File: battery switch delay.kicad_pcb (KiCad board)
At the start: 2 copper layers, 35.5 x 56 mm, 15 parts, among them J1 5mm pitch 4 position screw te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, K2 G6E-134P-US, Q1 Q_NPN, U2 MIC2920A-12WS-TR_SOT223

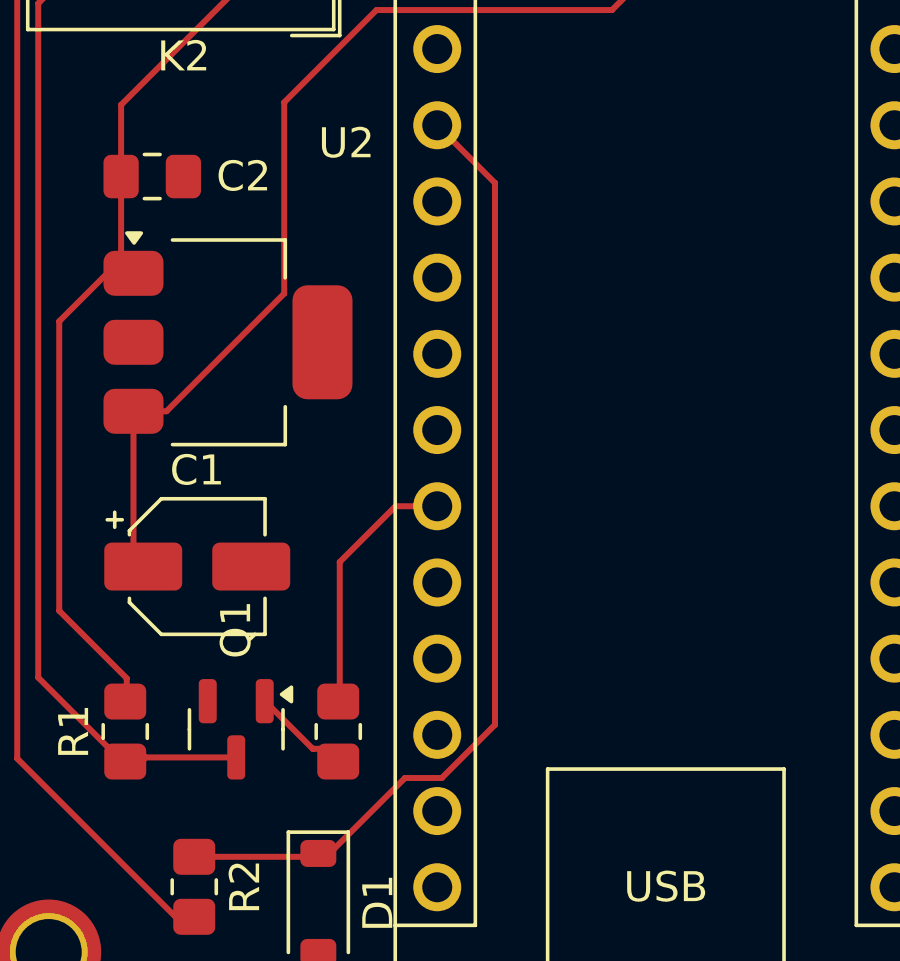
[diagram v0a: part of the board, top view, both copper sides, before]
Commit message: changed relay to smth with a much lower price .63 vs /bin/zsh.70 🤯
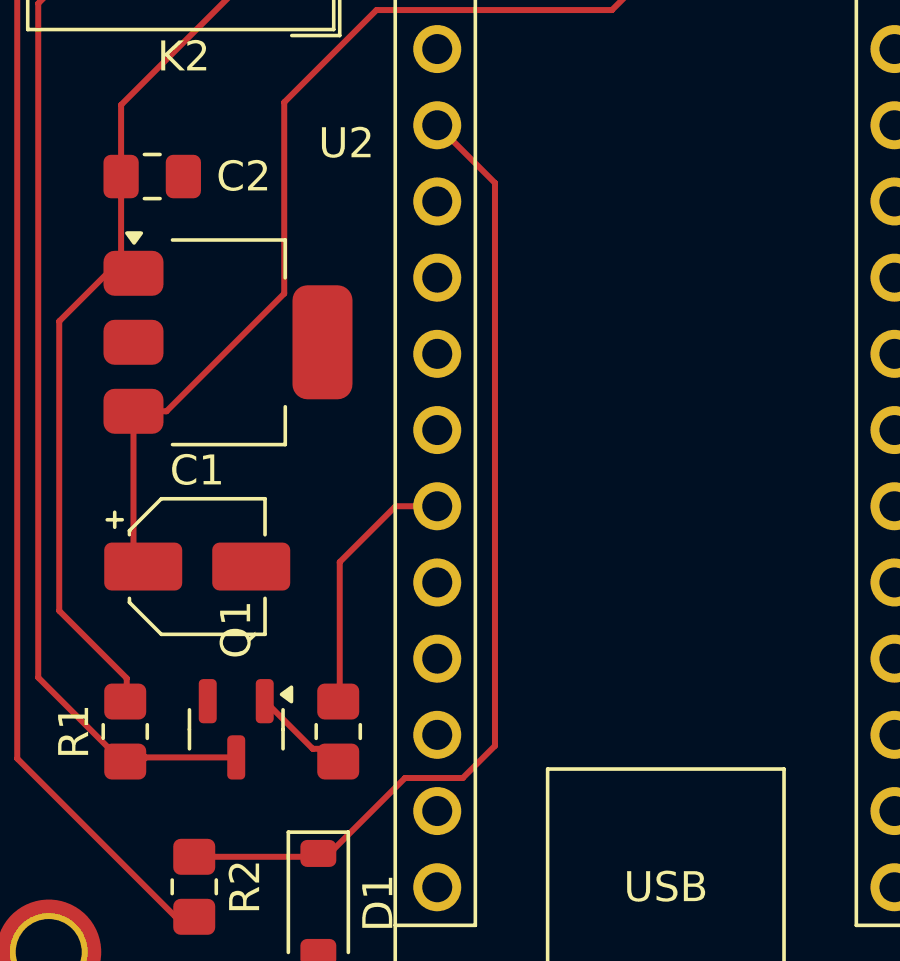
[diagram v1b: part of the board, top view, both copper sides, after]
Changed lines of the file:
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@@
 	)
 	(segment
-		(start 125.625 103.175)
-		(end 125.625 85.115)
+		(start 119.625 107.575529)
+		(end 119.7375 107.463029)
 		(width 0.2)
 		(layer "F.Cu")
@@
 	)
 	(segment
-		(start 119.625 107.575529)
-		(end 119.7375 107.463029)
+		(start 120.111971 107.463029)
+		(end 122.626 104.949)
+		(width 0.2)
+		(layer "F.Cu")
+		(net 2)
+	)
+	(segment
+		(start 122.626 104.949)
+		(end 124.551 104.949)
 		(width 0.2)
 		(layer "F.Cu")
@@
 	)
 	(segment
-		(start 123.851 104.949)
-		(end 125.625 103.175)
+		(start 124.551 104.949)
+		(end 125.625 103.875)
 		(width 0.2)
 		(layer "F.Cu")
@@
 	)
 	(segment
-		(start 125.625 85.115)
-		(end 123.7 83.19)
+		(start 125.625 103.875)
+		(end 125.625 85.115)
 		(width 0.2)
 		(layer "F.Cu")
@@
 	)
 	(segment
-		(start 122.626 104.949)
-		(end 123.851 104.949)
+		(start 125.625 85.115)
+		(end 123.7 83.19)
 		(width 0.2)
 		(layer "F.Cu")
-		(net 2)
-	)
-	(segment
-		(start 120.111971 107.463029)
-		(end 122.626 104.949)
-		(width 0.2)
-		(layer "F.Cu")

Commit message: test commit
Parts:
- removed K2: G6E-134P-US, Relay_THT:Relay_SPDT_Omron_G6E
- added K1: FINDER-36.11, Relay_THT:Relay_SPDT_Finder_36.11, F.Cu at (118.7, 78.3)
- moved REF** 4.50 mm to (106.2, 58.2)
- moved REF** 4.50 mm to (106.2, 110.8)
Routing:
- net Net-(Q1-C): track 31.7 -> 48.2 mm
- net to switch: track 22.9 -> 34.3 mm
- net ctrl: track 67.2 -> 70.1 mm
- net +12V: track 65.8 -> 67.1 mm
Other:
- board size 35.5 x 56 mm -> 40 x 56 mm

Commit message: debuging kicanvas
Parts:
- moved K1 1.30 mm to (118.7, 77.0)
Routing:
- net ctrl: track 70.1 -> 71.9 mm
- net to switch: track 34.3 -> 33.0 mm
- net Net-(Q1-C): track 48.2 -> 49.5 mm
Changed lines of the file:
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@@
 	(footprint "Relay_THT:Relay_SPDT_Finder_36.11"
 		(layer "F.Cu")
-		(at 118.7 78.3 180)
+		(at 118.7 77 180)
 		(descr "FINDER 36.11, SPDT relay, 10A, https://cdn.findernet.com/app/uploads/S36EN.pdf")
 		(tags "spdt relay")
@@
 	)
 	(segment
+		(start 112.7 67.9)
+		(end 112.7 79)
+		(width 0.2)
+		(layer "F.Cu")
+		(net 30)
+	)
+	(segment
 		(start 131.7 60.8)
 		(end 129.325 63.175)
@@
 	)
 	(segment
-		(start 112.7 67.9)
-		(end 112.7 80.3)
-		(width 0.2)
-		(layer "F.Cu")
-		(net 30)
-	)
-	(segment
 		(start 129.325 63.175)
 		(end 117.425 63.175)
@@
 	)
 	(segment
+		(start 106.7 64.8)
+		(end 108 66.1)
+		(width 0.2)
+		(layer "F.Cu")
+		(net 31)
+	)
+	(segment
+		(start 106.7 69.3)
+		(end 109.5 72.1)
+		(width 0.2)
+		(layer "F.Cu")
+		(net 31)
+	)
+	(segment
+		(start 115.320101 62.375)
+		(end 125.125 62.375)
+		(width 0.2)
+		(layer "F.Cu")
+		(net 31)
+	)
+	(segment
+		(start 125.125 62.375)
+		(end 126.7 60.8)
+		(width 0.2)
+		(layer "F.Cu")
+		(net 31)
+	)
+	(segment
+		(start 108 66.1)
+		(end 111.595101 66.1)
+		(width 0.2)
+		(layer "F.Cu")
+		(net 31)
+	)
+	(segment
 		(start 114.375529 109.575529)
 		(end 115.6 109.575529)
@@
 	)
 	(segment
+		(start 106.7 64.8)
+		(end 106.7 69.3)
+		(width 0.2)
+		(layer "F.Cu")
+		(net 31)
+	)
+	(segment
+		(start 109.5 72.1)
+		(end 109.5 104.7)
+		(width 0.2)
+		(layer "F.Cu")
+		(net 31)
+	)
+	(segment
+		(start 111.595101 66.1)
+		(end 115.320101 62.375)
+		(width 0.2)
+		(layer "F.Cu")
+		(net 31)
+	)
+	(segment
 		(start 109.5 104.7)
 		(end 114.375529 109.575529)
@@
 	)
 	(segment
-		(start 115.320101 62.375)
-		(end 125.125 62.375)
-		(width 0.2)
-		(layer "F.Cu")
-		(net 31)
-	)
-	(segment
-		(start 125.125 62.375)
-		(end 126.7 60.8)
-		(width 0.2)
-		(layer "F.Cu")
-		(net 31)
-	)
-	(segment
-		(start 106.7 69.3)
-		(end 109.5 72.1)
-		(width 0.2)
-		(layer "F.Cu")
-		(net 31)
-	)
-	(segment
-		(start 106.7 66.1)
-		(end 106.7 69.3)
-		(width 0.2)
-		(layer "F.Cu")
-		(net 31)
-	)
-	(segment
-		(start 111.595101 66.1)
-		(end 115.320101 62.375)
-		(width 0.2)
-		(layer "F.Cu")
-		(net 31)
-	)
-	(segment
-		(start 109.5 72.1)
-		(end 109.5 104.7)
-		(width 0.2)
-		(layer "F.Cu")
-		(net 31)
-	)
-	(segment
-		(start 106.7 66.1)
-		(end 111.595101 66.1)
-		(width 0.2)
-		(layer "F.Cu")
-		(net 31)
-	)
-	(segment
 		(start 115.4 82.9)
 		(end 113.4 84.9)
@@
 	)
 	(segment
+		(start 118.7 69.8)
+		(end 121.725 66.775)
+		(width 0.2)
+		(layer "F.Cu")
+		(net 32)
+	)
+	(segment
 		(start 111.8 102.4)
 		(end 111.1 101.7)
@@
 	)
 	(segment
+		(start 118.7 77)
+		(end 118.7 81.6)
+		(width 0.2)
+		(layer "F.Cu")
+		(net 32)
+	)
+	(segment
+		(start 112.7 88.125)
+		(end 113.575 88.125)
+		(width 0.2)
+		(layer "F.Cu")
+		(net 32)
+	)
+	(segment
+		(start 118.7 77)
+		(end 118.7 69.8)
+		(width 0.2)
+		(layer "F.Cu")
+		(net 32)
+	)
+	(segment
 		(start 113.4 84.9)
 		(end 113.1625 84.9)
@@
 	)
 	(segment
-		(start 112.7 88.125)
-		(end 113.575 88.125)
-		(width 0.2)
-		(layer "F.Cu")
-		(net 32)
-	)
-	(segment
 		(start 111.1 89.725)
 		(end 112.7 88.125)
@@
 	)
 	(segment
+		(start 113.09085 85.52835)
+		(end 113.1625 85.4567)
+		(width 0.2)
+		(layer "F.Cu")
+		(net 32)
+	)
+	(segment
 		(start 117.4 82.9)
 		(end 115.4 82.9)
@@
 	)
 	(segment
-		(start 113.09085 85.52835)
-		(end 113.1625 85.4567)
-		(width 0.2)
-		(layer "F.Cu")
-		(net 32)
-	)
-	(segment
 		(start 111.1 101.7)
 		(end 111.1 89.725)
@@
 	)
 	(segment
+		(start 113.575 88.0375)
+		(end 113.1625 87.625)
+		(width 0.2)
+		(layer "F.Cu")
+		(net 32)
+	)
+	(segment
+		(start 135.725 66.775)
+		(end 141.7 60.8)
+		(width 0.2)
+		(layer "F.Cu")
+		(net 32)
+	)
+	(segment
+		(start 113.1625 85.4567)
+		(end 113.1625 84.9)
+		(width 0.2)
+		(layer "F.Cu")
+		(net 32)
+	)
+	(segment
+		(start 113.3 102.4)
+		(end 111.8 102.4)
+		(width 0.2)
+		(layer "F.Cu")
+		(net 32)
+	)
+	(segment
 		(start 118.7 81.6)
 		(end 117.4 82.9)
@@
 	)
 	(segment
-		(start 118.7 78.3)
-		(end 118.7 81.6)
-		(width 0.2)
-		(layer "F.Cu")
-		(net 32)
-	)
-	(segment
-		(start 113.575 88.0375)
-		(end 113.1625 87.625)
-		(width 0.2)
-		(layer "F.Cu")
-		(net 32)
-	)
-	(segment
-		(start 118.7 78.3)
-		(end 118.7 69.8)
-		(width 0.2)
-		(layer "F.Cu")
-		(net 32)
-	)
-	(segment
-		(start 113.1625 85.4567)
+		(start 113.1625 87.625)
 		(end 113.1625 84.9)
-		(width 0.2)
-		(layer "F.Cu")
-		(net 32)
-	)
-	(segment
-		(start 113.3 102.4)
-		(end 111.8 102.4)
 		(width 0.2)
 		(layer "F.Cu")
@@
 	)
 	(segment
-		(start 118.7 69.8)
-		(end 121.725 66.775)
-		(width 0.2)
-		(layer "F.Cu")
-		(net 32)
-	)
-	(segment
-		(start 135.725 66.775)
-		(end 141.7 60.8)
-		(width 0.2)
-		(layer "F.Cu")
-		(net 32)
-	)
-	(segment
-		(start 113.1625 87.625)
-		(end 113.1625 84.9)
-		(width 0.2)
-		(layer "F.Cu")
-		(net 32)
+		(start 110.3 84.5)
+		(end 110.3 102.5)
+		(width 0.2)
+		(layer "F.Cu")
+		(net 33)
+	)
+	(segment
+		(start 113.75 104.5)
+		(end 113.9875 104.2625)
+		(width 0.2)
+		(layer "F.Cu")
+		(net 33)
+	)
+	(segment
+		(start 113.3 82.6)
+		(end 112.2 82.6)
+		(width 0.2)
+		(layer "F.Cu")
+		(net 33)
+	)
+	(segment
+		(start 113.9875 104.2625)
+		(end 117 104.2625)
+		(width 0.2)
+		(layer "F.Cu")
+		(net 33)
+	)
+	(segment
+		(start 113.3 104.4)
+		(end 113.4 104.4)
+		(width 0.2)
+		(layer "F.Cu")
+		(net 33)
+	)
+	(segment
+		(start 118.7 64.8)
+		(end 118.7 66.1)
+		(width 0.2)
+		(layer "F.Cu")
+		(net 33)
+	)
+	(segment
+		(start 115.4 69.4)
+		(end 115.4 80.5)
+		(width 0.2)
+		(layer "F.Cu")
+		(net 33)
 	)
 	(segment
@@
 	)
 	(segment
-		(start 110.3 84.5)
-		(end 110.3 102.5)
+		(start 112.2 104.4)
+		(end 113.3 104.4)
+		(width 0.2)
+		(layer "F.Cu")
+		(net 33)
+	)
+	(segment
+		(start 110.3 102.5)
+		(end 112.2 104.4)
+		(width 0.2)
+		(layer "F.Cu")
+		(net 33)
+	)
+	(segment
+		(start 112.2 82.6)
+		(end 110.3 84.5)
 		(width 0.2)
 		(layer "F.Cu")
@@
 		(width 0.2)
 		(layer "F.Cu")
-		(net 33)
-	)
-	(segment
-		(start 113.75 104.5)
-		(end 113.9875 104.2625)
-		(width 0.2)
-		(layer "F.Cu")
-		(net 33)
-	)
-	(segment
-		(start 115.4 69.4)
-		(end 115.4 80.5)
-		(width 0.2)
-		(layer "F.Cu")
-		(net 33)
-	)
-	(segment
-		(start 113.9875 104.2625)
-		(end 117 104.2625)
-		(width 0.2)
-		(layer "F.Cu")
-		(net 33)
-	)
-	(segment
-		(start 113.3 104.4)
-		(end 113.4 104.4)
-		(width 0.2)
-		(layer "F.Cu")
-		(net 33)
-	)
-	(segment
-		(start 112.2 82.6)
-		(end 110.3 84.5)
-		(width 0.2)
-		(layer "F.Cu")
-		(net 33)
-	)
-	(segment
-		(start 112.2 104.4)
-		(end 113.3 104.4)
-		(width 0.2)
-		(layer "F.Cu")
-		(net 33)
-	)
-	(segment
-		(start 113.3 82.6)
-		(end 112.2 82.6)
-		(width 0.2)
-		(layer "F.Cu")
-		(net 33)
-	)
-	(segment
-		(start 110.3 102.5)
-		(end 112.2 104.4)
-		(width 0.2)
-		(layer "F.Cu")

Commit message: debuging kicanvas
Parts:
- moved K1 1.30 mm to (118.7, 78.3)
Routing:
- net ctrl: track 71.9 -> 70.1 mm
- net to switch: track 33.0 -> 34.3 mm
- net Net-(Q1-C): track 49.5 -> 48.2 mm
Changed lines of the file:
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@@
 	(footprint "Relay_THT:Relay_SPDT_Finder_36.11"
 		(layer "F.Cu")
-		(at 118.7 77 180)
+		(at 118.7 78.3 180)
 		(descr "FINDER 36.11, SPDT relay, 10A, https://cdn.findernet.com/app/uploads/S36EN.pdf")
 		(tags "spdt relay")
@@
 	(segment
 		(start 112.7 67.9)
-		(end 112.7 79)
+		(end 112.7 80.3)
 		(width 0.2)
 		(layer "F.Cu")
@@
 	)
 	(segment
+		(start 129.325 63.175)
+		(end 117.425 63.175)
+		(width 0.2)
+		(layer "F.Cu")
+		(net 30)
+	)
+	(segment
 		(start 117.425 63.175)
 		(end 112.7 67.9)
@@
 	)
 	(segment
-		(start 129.325 63.175)
-		(end 117.425 63.175)
-		(width 0.2)
-		(layer "F.Cu")
-		(net 30)
-	)
-	(segment
-		(start 106.7 64.8)
-		(end 108 66.1)
+		(start 114.375529 109.575529)
+		(end 115.6 109.575529)
 		(width 0.2)
 		(layer "F.Cu")
@@
 	)
 	(segment
+		(start 106.7 66.1)
+		(end 111.595101 66.1)
+		(width 0.2)
+		(layer "F.Cu")
+		(net 31)
+	)
+	(segment
+		(start 106.7 66.1)
+		(end 106.7 69.3)
+		(width 0.2)
+		(layer "F.Cu")
+		(net 31)
+	)
+	(segment
+		(start 109.5 72.1)
+		(end 109.5 104.7)
+		(width 0.2)
+		(layer "F.Cu")
+		(net 31)
+	)
+	(segment
+		(start 109.5 104.7)
+		(end 114.375529 109.575529)
+		(width 0.2)
+		(layer "F.Cu")
+		(net 31)
+	)
+	(segment
+		(start 125.125 62.375)
+		(end 126.7 60.8)
+		(width 0.2)
+		(layer "F.Cu")
+		(net 31)
+	)
+	(segment
 		(start 115.320101 62.375)
 		(end 125.125 62.375)
@@
 	)
 	(segment
-		(start 125.125 62.375)
-		(end 126.7 60.8)
-		(width 0.2)
-		(layer "F.Cu")
-		(net 31)
-	)
-	(segment
-		(start 108 66.1)
-		(end 111.595101 66.1)
-		(width 0.2)
-		(layer "F.Cu")
-		(net 31)
-	)
-	(segment
-		(start 114.375529 109.575529)
-		(end 115.6 109.575529)
-		(width 0.2)
-		(layer "F.Cu")
-		(net 31)
-	)
-	(segment
-		(start 106.7 64.8)
-		(end 106.7 69.3)
-		(width 0.2)
-		(layer "F.Cu")
-		(net 31)
-	)
-	(segment
-		(start 109.5 72.1)
-		(end 109.5 104.7)
-		(width 0.2)
-		(layer "F.Cu")
-		(net 31)
-	)
-	(segment
 		(start 111.595101 66.1)
 		(end 115.320101 62.375)
@@
 	)
 	(segment
-		(start 109.5 104.7)
-		(end 114.375529 109.575529)
-		(width 0.2)
-		(layer "F.Cu")
-		(net 31)
+		(start 118.7 78.3)
+		(end 118.7 69.8)
+		(width 0.2)
+		(layer "F.Cu")
+		(net 32)
+	)
+	(segment
+		(start 118.7 78.3)
+		(end 118.7 81.6)
+		(width 0.2)
+		(layer "F.Cu")
+		(net 32)
+	)
+	(segment
+		(start 121.725 66.775)
+		(end 135.725 66.775)
+		(width 0.2)
+		(layer "F.Cu")
+		(net 32)
+	)
+	(segment
+		(start 111.8 102.4)
+		(end 111.1 101.7)
+		(width 0.2)
+		(layer "F.Cu")
+		(net 32)
+	)
+	(segment
+		(start 113.575 88.125)
+		(end 113.575 88.0375)
+		(width 0.2)
+		(layer "F.Cu")
+		(net 32)
+	)
+	(segment
+		(start 118.7 69.8)
+		(end 121.725 66.775)
+		(width 0.2)
+		(layer "F.Cu")
+		(net 32)
+	)
+	(segment
+		(start 117.4 82.9)
+		(end 115.4 82.9)
+		(width 0.2)
+		(layer "F.Cu")
+		(net 32)
 	)
 	(segment
@@
 	)
 	(segment
-		(start 118.7 69.8)
-		(end 121.725 66.775)
-		(width 0.2)
-		(layer "F.Cu")
-		(net 32)
-	)
-	(segment
-		(start 111.8 102.4)
-		(end 111.1 101.7)
-		(width 0.2)
-		(layer "F.Cu")
-		(net 32)
-	)
-	(segment
-		(start 113.575 88.125)
-		(end 113.575 88.0375)
-		(width 0.2)
-		(layer "F.Cu")
-		(net 32)
-	)
-	(segment
-		(start 118.7 77)
-		(end 118.7 81.6)
+		(start 135.725 66.775)
+		(end 141.7 60.8)
 		(width 0.2)
 		(layer "F.Cu")
@@
 	)
 	(segment
-		(start 118.7 77)
-		(end 118.7 69.8)
+		(start 111.1 89.725)
+		(end 112.7 88.125)
+		(width 0.2)
+		(layer "F.Cu")
+		(net 32)
+	)
+	(segment
+		(start 113.09085 85.52835)
+		(end 113.1625 85.4567)
+		(width 0.2)
+		(layer "F.Cu")
+		(net 32)
+	)
+	(segment
+		(start 118.7 81.6)
+		(end 117.4 82.9)
+		(width 0.2)
+		(layer "F.Cu")
+		(net 32)
+	)
+	(segment
+		(start 111.1 101.7)
+		(end 111.1 89.725)
+		(width 0.2)
+		(layer "F.Cu")
+		(net 32)
+	)
+	(segment
+		(start 113.575 88.0375)
+		(end 113.1625 87.625)
 		(width 0.2)
 		(layer "F.Cu")
@@
 	)
 	(segment
-		(start 111.1 89.725)
-		(end 112.7 88.125)
-		(width 0.2)
-		(layer "F.Cu")
-		(net 32)
-	)
-	(segment
-		(start 113.09085 85.52835)
-		(end 113.1625 85.4567)
-		(width 0.2)
-		(layer "F.Cu")
-		(net 32)
-	)
-	(segment
-		(start 117.4 82.9)
-		(end 115.4 82.9)
-		(width 0.2)
-		(layer "F.Cu")
-		(net 32)
-	)
-	(segment
-		(start 111.1 101.7)
-		(end 111.1 89.725)
-		(width 0.2)
-		(layer "F.Cu")
-		(net 32)
-	)
-	(segment
-		(start 113.575 88.0375)
-		(end 113.1625 87.625)
-		(width 0.2)
-		(layer "F.Cu")
-		(net 32)
-	)
-	(segment
-		(start 135.725 66.775)
-		(end 141.7 60.8)
-		(width 0.2)
-		(layer "F.Cu")
-		(net 32)
-	)
-	(segment
 		(start 113.1625 85.4567)
 		(end 113.1625 84.9)
@@
 	)
 	(segment
-		(start 118.7 81.6)
-		(end 117.4 82.9)
-		(width 0.2)
-		(layer "F.Cu")
-		(net 32)
-	)
-	(segment
 		(start 113.1625 87.625)
 		(end 113.1625 84.9)
@@
 	)
 	(segment
-		(start 121.725 66.775)
-		(end 135.725 66.775)
-		(width 0.2)
-		(layer "F.Cu")
-		(net 32)
+		(start 113.75 104.5)
+		(end 113.9875 104.2625)
+		(width 0.2)
+		(layer "F.Cu")
+		(net 33)
+	)
+	(segment
+		(start 118.7 66.1)
+		(end 115.4 69.4)
+		(width 0.2)
+		(layer "F.Cu")
+		(net 33)
+	)
+	(segment
+		(start 113.9875 104.2625)
+		(end 117 104.2625)
+		(width 0.2)
+		(layer "F.Cu")
+		(net 33)
+	)
+	(segment
+		(start 113.3 82.6)
+		(end 112.2 82.6)
+		(width 0.2)
+		(layer "F.Cu")
+		(net 33)
+	)
+	(segment
+		(start 113.3 104.4)
+		(end 113.4 104.4)
+		(width 0.2)
+		(layer "F.Cu")
+		(net 33)
+	)
+	(segment
+		(start 112.2 82.6)
+		(end 110.3 84.5)
+		(width 0.2)
+		(layer "F.Cu")
+		(net 33)
+	)
+	(segment
+		(start 112.2 104.4)
+		(end 113.3 104.4)
+		(width 0.2)
+		(layer "F.Cu")
+		(net 33)
 	)
 	(segment
@@
 	)
 	(segment
-		(start 113.75 104.5)
-		(end 113.9875 104.2625)
-		(width 0.2)
-		(layer "F.Cu")
-		(net 33)
-	)
-	(segment
-		(start 113.3 82.6)
-		(end 112.2 82.6)
-		(width 0.2)
-		(layer "F.Cu")
-		(net 33)
-	)
-	(segment
-		(start 113.9875 104.2625)
-		(end 117 104.2625)
-		(width 0.2)
-		(layer "F.Cu")
-		(net 33)
-	)
-	(segment
-		(start 113.3 104.4)
-		(end 113.4 104.4)
-		(width 0.2)
-		(layer "F.Cu")
-		(net 33)
-	)
-	(segment
-		(start 118.7 64.8)
-		(end 118.7 66.1)
-		(width 0.2)
-		(layer "F.Cu")
-		(net 33)
-	)
-	(segment
 		(start 115.4 69.4)
 		(end 115.4 80.5)
@@
 	)
 	(segment
-		(start 118.7 66.1)
-		(end 115.4 69.4)
+		(start 115.4 80.5)
+		(end 113.3 82.6)
 		(width 0.2)
 		(layer "F.Cu")
@@
 	)
 	(segment
-		(start 112.2 104.4)
-		(end 113.3 104.4)
+		(start 113.4 104.4)
+		(end 113.5 104.5)
 		(width 0.2)
 		(layer "F.Cu")
@@
 		(width 0.2)
 		(layer "F.Cu")
-		(net 33)
-	)
-	(segment
-		(start 112.2 82.6)
-		(end 110.3 84.5)
-		(width 0.2)
-		(layer "F.Cu")
-		(net 33)
-	)
-	(segment
-		(start 115.4 80.5)
-		(end 113.3 82.6)
-		(width 0.2)
-		(layer "F.Cu")
-		(net 33)
-	)
-	(segment
-		(start 113.4 104.4)
-		(end 113.5 104.5)
-		(width 0.2)
-		(layer "F.Cu")
